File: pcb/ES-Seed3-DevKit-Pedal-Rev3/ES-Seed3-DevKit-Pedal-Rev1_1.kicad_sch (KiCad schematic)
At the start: 17 parts, among them J7 USB4110GFA, U11 H11L1, U14 USBLC6-2SC6

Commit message: first review/prod folders after making all changes.
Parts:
- added QR1: ~, shnsly:qr-seed3-desktop-redirect-medium, symbol shnsly:QR-Code
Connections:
- net SDMMC_DETECT: now reaches A1.12 (I2C1_SCL)
- no-connect marks 0 -> 7

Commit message: boxes around daisy pins, osh logo fix, etc.
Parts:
- LOGO1: footprint parts-for-kicad:OSHW-LOGO-L_TEXT -> Symbol:OSHW-Logo2_14.6x12mm_SilkScreen
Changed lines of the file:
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@@
 			)
 		)
-		(property "Footprint" "parts-for-kicad:OSHW-LOGO-L_TEXT"
+		(property "Footprint" "Symbol:OSHW-Logo2_14.6x12mm_SilkScreen"
 			(at 152.4 212.09 0)
 			(effects

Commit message: prod mats with last bits of silk adjustment.
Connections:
- net TAC_SW1 renamed TAC_SW4
- net TAC_SW2 renamed TAC_SW5
- net TOG_1 renamed TOG_SW2
- net TOG_2_A renamed TOG_SW1_A
- net TOG_2_B renamed TOG_SW1_B
- net TOG_3 renamed TOG_SW3
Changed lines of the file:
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@@
 		)
 	)
-	(global_label "TAC_SW2"
+	(global_label "TAC_SW5"
 		(shape input)
 		(at 76.2 130.81 180)
@@
 		)
 	)
-	(global_label "TOG_1"
+	(global_label "TOG_SW2"
 		(shape bidirectional)
 		(at 139.7 110.49 0)
@@
 		)
 		(property "Intersheetrefs" "${INTERSHEET_REFS}"
-			(at 149.3446 110.49 0)
-			(effects
-				(font
-					(size 1.27 1.27)
-				)
-				(justify left)
-				(hide yes)
-			)
-		)
-	)
-	(global_label "TAC_SW1"
+			(at 151.9523 110.49 0)
+			(effects
+				(font
+					(size 1.27 1.27)
+				)
+				(justify left)
+				(hide yes)
+			)
+		)
+	)
+	(global_label "TAC_SW4"
 		(shape bidirectional)
 		(at 138.43 78.74 0)
@@
 		)
 	)
-	(global_label "TOG_2_B"
+	(global_label "TOG_SW1_B"
 		(shape bidirectional)
 		(at 139.7 105.41 0)
@@
 		)
 		(property "Intersheetrefs" "${INTERSHEET_REFS}"
-			(at 151.5375 105.41 0)
+			(at 154.1452 105.41 0)
 			(effects
 				(font
@@
 		)
 	)
-	(global_label "TOG_3"
+	(global_label "TOG_SW3"
 		(shape input)
 		(at 76.2 113.03 180)
@@
 		)
 		(property "Intersheetrefs" "${INTERSHEET_REFS}"
-			(at 65.0506 113.03 0)
+			(at 64.8087 113.03 0)
 			(effects
 				(font
@@
 		)
 	)
-	(global_label "TOG_2_A"
+	(global_label "TOG_SW1_A"
 		(shape bidirectional)
 		(at 139.7 107.95 0)
@@
 		)
 		(property "Intersheetrefs" "${INTERSHEET_REFS}"
-			(at 151.3597 107.95 0)
-			(effects
-				(font
+			(at 153.9674 107.95 0)
+			(effects
+				(font

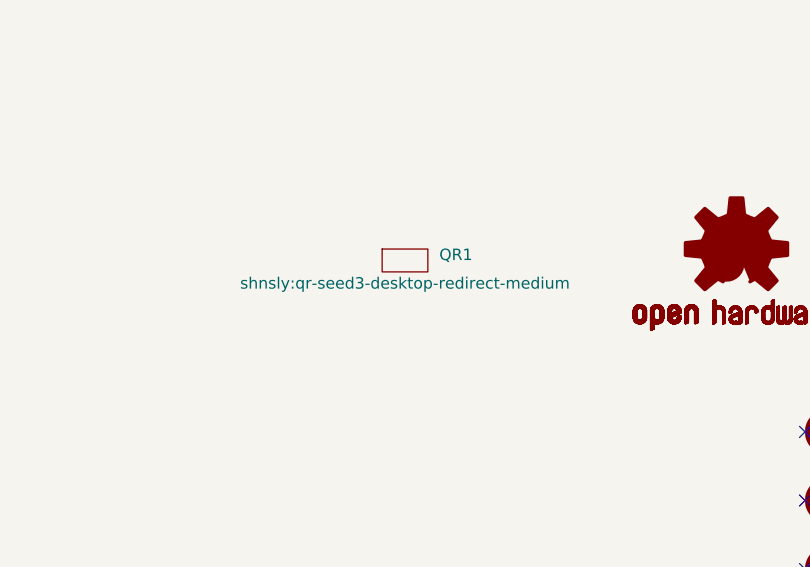
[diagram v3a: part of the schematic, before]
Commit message: fixed QR code to be correct destination link, and removed DNIs.
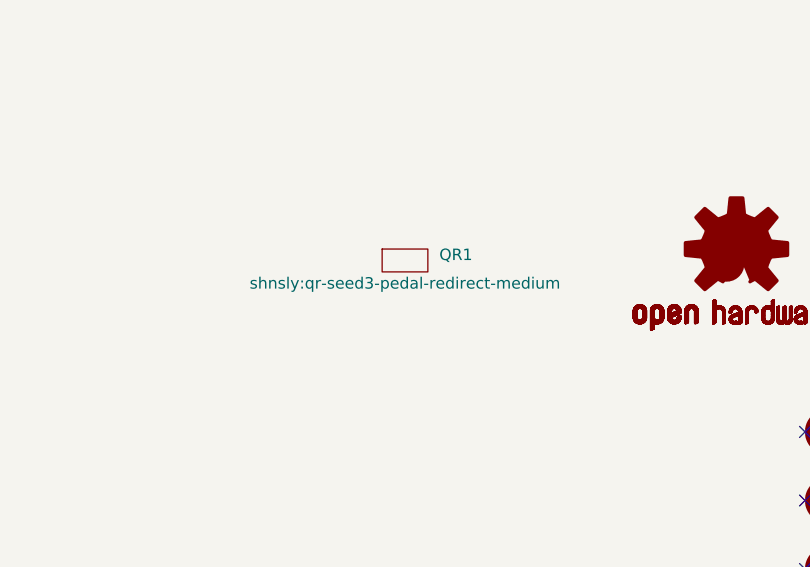
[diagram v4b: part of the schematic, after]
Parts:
- QR1: footprint shnsly:qr-seed3-desktop-redirect-medium -> shnsly:qr-seed3-pedal-redirect-medium
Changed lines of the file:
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@@
 			)
 		)
-		(property "Footprint" "shnsly:qr-seed3-desktop-redirect-medium"
+		(property "Footprint" "shnsly:qr-seed3-pedal-redirect-medium"
 			(at 115.57 215.9 0)
 			(effects
